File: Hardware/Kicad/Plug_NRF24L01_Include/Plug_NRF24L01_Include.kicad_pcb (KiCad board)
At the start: 2 copper layers, 55 x 40 mm, 43 parts, among them J1 Conn_01x07_Socket, Q1 2N7002, Q2 2N7002, Q3 2N7002, SW1 SW_Push, U1 NRF24L01, U2 AMS1117-3.3, U3 STM32L412KBTx, Y1 16 MHz

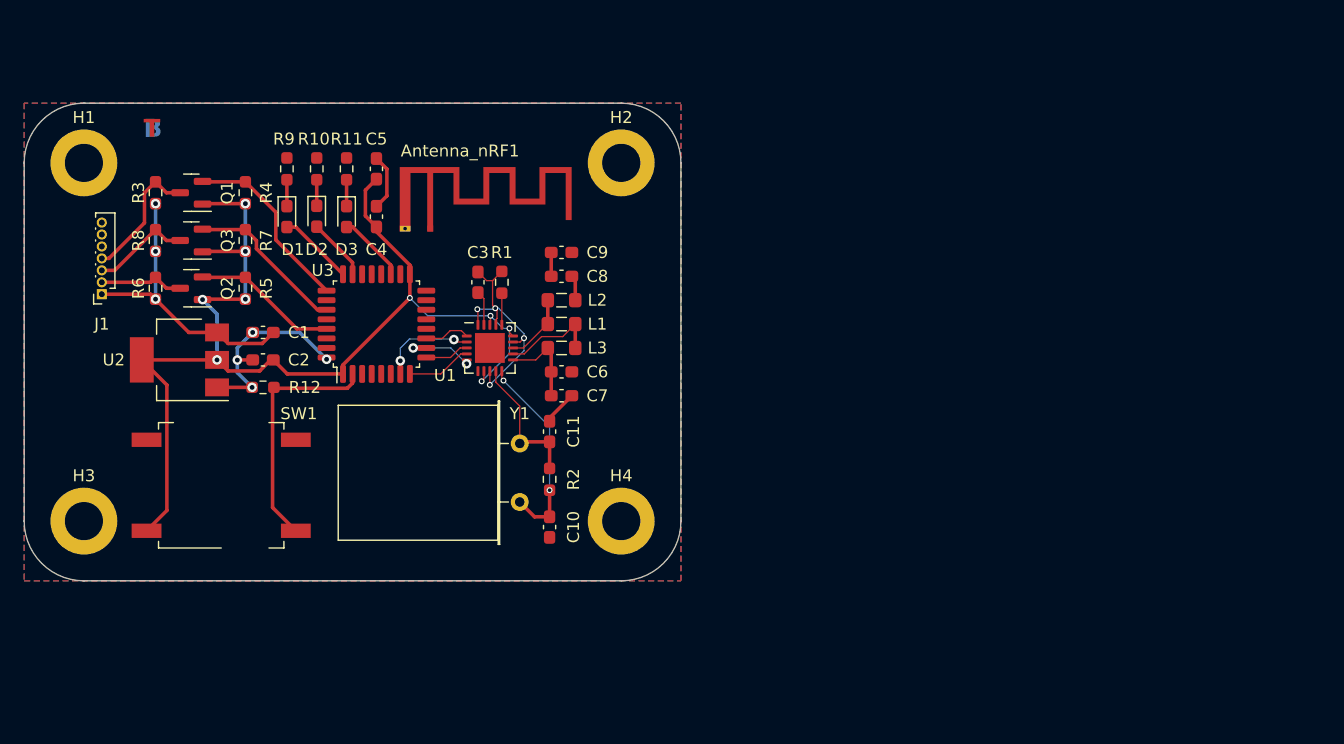
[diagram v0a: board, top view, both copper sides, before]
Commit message: Updated NRF24L01_Include
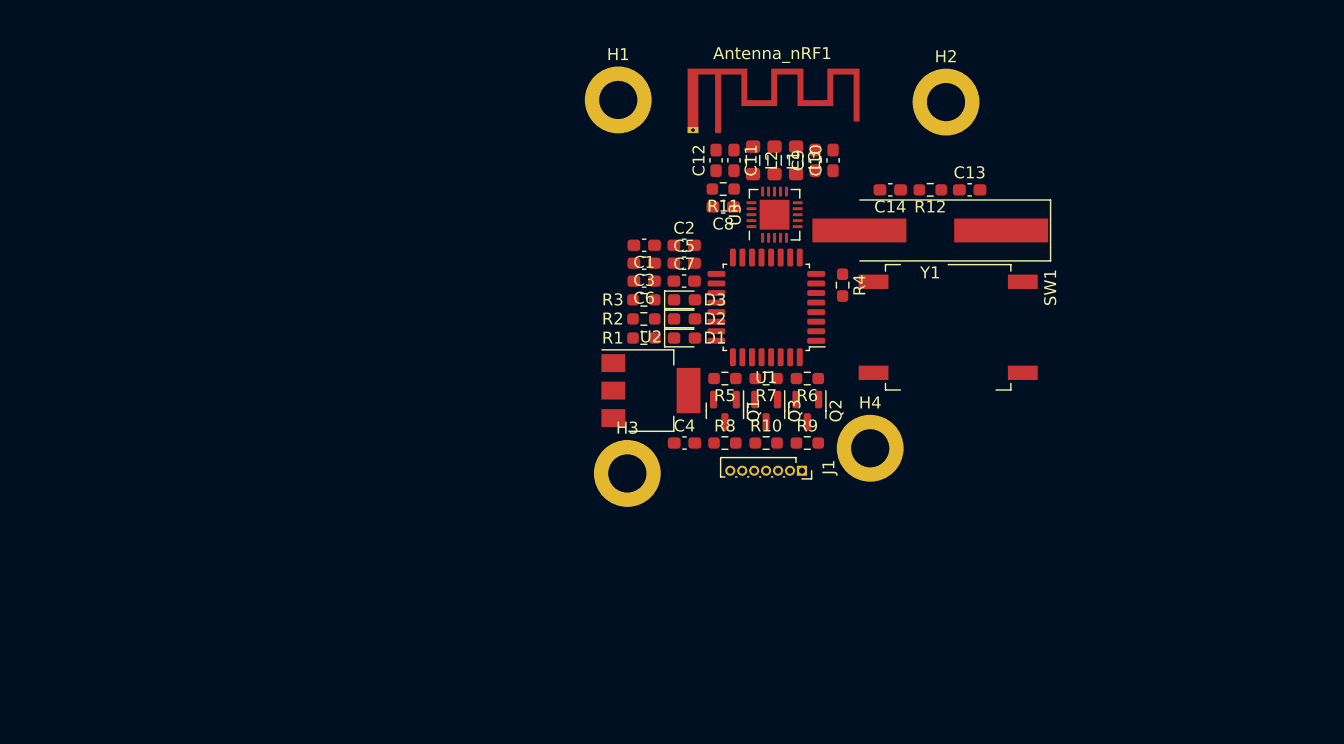
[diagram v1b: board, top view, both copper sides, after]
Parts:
- added C12: 1.0p, Capacitor_SMD:C_0603_1608Metric_Pad1.08x0.95mm_HandSolder, F.Cu at (100.9, 62.8)
- added C13: 22p, Capacitor_SMD:C_0603_1608Metric_Pad1.08x0.95mm_HandSolder, F.Cu at (122.2, 65.3)
- added C14: 22p, Capacitor_SMD:C_0603_1608Metric_Pad1.08x0.95mm_HandSolder, F.Cu at (115.5, 65.3)
- C1, C2: value 1u -> 100n
- C10: value 22p -> 4.7p
- C11: value 22p -> 1.5p
- C3: value 33n -> 100n
- C4: value 10n -> 1u
- C5: value 1n -> 1u
- C6: value 2.2n -> 10n
- C7: value 4.7p -> 1n
- C8: value 1.5p -> 33n
- C9: value 1.0p -> 2.2n
- R1: value 22k -> 1k
- R10, R9: value 1k -> 10k
- R11: value 1k -> 22k
- R12: value 10k -> 1M
- R2: value 1M -> 1k
- R3: value 10k -> 1k
- U1: value NRF24L01 -> STM32L412KBTx; footprint Package_DFN_QFN:QFN-20-1EP_4x4mm_P0.5mm_EP2.5x2.5mm -> Package_QFP:LQFP-32_7x7mm_P0.8mm
- U3: value STM32L412KBTx -> nRF24L01P; footprint Package_QFP:LQFP-32_7x7mm_P0.8mm -> Package_DFN_QFN:QFN-20-1EP_4x4mm_P0.5mm_EP2.5x2.5mm
- Y1: value 16 MHz -> 16MHz; footprint Crystal:Crystal_HC49-U_Horizontal -> Crystal:Crystal_SMD_HC49-SD_HandSoldering
- moved SW1 62.3 mm to (120.4, 76.8), turned to -90 degrees
- moved J1 60.5 mm to (108.1, 88.8), turned to -90 degrees
- moved R12 58.3 mm to (118.9, 65.3)
- moved R6 55.1 mm to (108.6, 81.1), turned to 180 degrees
- moved Q2 52.6 mm to (108.6, 83.8), turned to -90 degrees
- moved R4 50.6 mm to (111.5, 73.2), turned to -90 degrees
- moved R8 50.6 mm to (101.7, 86.5), turned to 0 degrees
- moved Q3 50.2 mm to (105.1, 83.8), turned to -90 degrees
- moved R9 49.3 mm to (108.6, 86.5), turned to 0 degrees
- moved Q1 48.3 mm to (101.7, 83.8), turned to -90 degrees
- moved H3 45.7 mm to (93.5, 89.0)
- moved R7 45.1 mm to (105.1, 81.1), turned to 180 degrees
- moved H1 45.1 mm to (92.8, 57.7)
- moved R10 44.1 mm to (105.1, 86.5), turned to 0 degrees
- moved R3 41.9 mm to (94.9, 74.5), turned to 180 degrees
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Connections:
- C1 pad 1: +5V -> +3.3V
- C10 pad 1: XC1 -> VDD_PA
- C11 pad 1: XC2 -> RF_Output
- C11 pad 2: GND -> Net-(C11-Pad2)
- C2 pad 1: VDD_NRF -> +3.3V
- C3 pad 1: Net-(U1-DVDD) -> +3.3V
- C3 pad 2: GND1 -> GND
- C4 pad 1: VDD_NRF -> +5V
- C5 pad 1: VDD_NRF -> +3.3V
- C6 pad 1: VDD_PA -> +3.3V
- C7 pad 1: VDD_PA -> +3.3V
- C8 pad 1: RF_Output -> Net-(U3-DVDD)
- C8 pad 2: Net-(C8-Pad2) -> GND1
- C9 pad 1: GND -> VDD_PA
- C9 pad 2: RF_Output -> GND
- L2 pad 2: Net-(C8-Pad2) -> Net-(C11-Pad2)
- Q1 pad 1: VDD_NRF -> +3.3V
- Q2 pad 1: VDD_NRF -> +3.3V
- Q3 pad 1: VDD_NRF -> +3.3V
- R1 pad 1: Net-(U1-IREF) -> Net-(D1-K)
- R1 pad 2: GND1 -> GND
- R10 pad 1: Net-(D2-K) -> +5V
- R10 pad 2: GND -> Data_Latch_SNES
- R11 pad 1: Net-(D3-K) -> Net-(U3-IREF)
- R11 pad 2: GND -> GND1
- R12 pad 1: Appairing_Btn -> XC1
- R12 pad 2: GND -> XC2
- R2 pad 1: XC1 -> Net-(D2-K)
- R2 pad 2: XC2 -> GND
- R3 pad 1: +5V -> Net-(D3-K)
- R3 pad 2: Serial_Data_SNES -> GND
- R4 pad 1: VDD_NRF -> Appairing_Btn
- R4 pad 2: Serial_Data_STM32 -> GND
- R5 pad 1: VDD_NRF -> +3.3V
- R5 pad 2: Data_Clock_STM32 -> Serial_Data_STM32
- R6 pad 1: +5V -> +3.3V
- R6 pad 2: Data_Clock_SNES -> Data_Clock_STM32
- R7 pad 1: VDD_NRF -> +3.3V
- R8 pad 2: Data_Latch_SNES -> Serial_Data_SNES
- R9 pad 1: Net-(D1-K) -> +5V
- R9 pad 2: GND -> Data_Clock_SNES
- SW1 pad 1: VDD_NRF -> +3.3V
- U1 pad 1: Chip_Enable -> +3.3V
- U1 pad 10: XC1 -> SPI_Digital_Output
- U1 pad 11: VDD_PA -> Chip_Enable
- U1 pad 12: ANT1 -> unconnected-(U1-PA6-Pad12)
- U1 pad 13: ANT2 -> unconnected-(U1-PA7-Pad13)
- U1 pad 14: GND1 -> unconnected-(U1-PB0-Pad14)
- U1 pad 15: VDD_NRF -> unconnected-(U1-PB1-Pad15)
- U1 pad 16: Net-(U1-IREF) -> GND
- U1 pad 17: GND1 -> +3.3V
- U1 pad 18: VDD_NRF -> unconnected-(U1-PA8-Pad18)
- U1 pad 19: Net-(U1-DVDD) -> Status_LED
- U1 pad 2: SPI_Chip_Select -> Appairing_Btn
- U1 pad 20: GND1 -> unconnected-(U1-PA10-Pad20)
- U1 pad 21: (no net) -> unconnected-(U1-PA11-Pad21)
- U1 pad 3: SPI_Clock -> unconnected-(U1-PC15-Pad3)
- U1 pad 4: SPI_Digital_Input -> unconnected-(U1-NRST-Pad4)
- U1 pad 5: SPI_Digital_Output -> +3.3V
- U1 pad 7: VDD_NRF -> SPI_Chip_Select
- U1 pad 8: GND1 -> SPI_Digital_Input
- U1 pad 9: XC2 -> SPI_Clock
- U2 pad 2: VDD_NRF -> +3.3V
- U3 pad 1: VDD_NRF -> Chip_Enable
- U3 pad 10: SPI_Digital_Output -> XC1
- U3 pad 11: Chip_Enable -> VDD_PA
- U3 pad 12: unconnected-(U3-PA6-Pad12) -> ANT1
- U3 pad 13: unconnected-(U3-PA7-Pad13) -> ANT2
- U3 pad 14: unconnected-(U3-PB0-Pad14) -> GND1
- U3 pad 15: unconnected-(U3-PB1-Pad15) -> +3.3V
- U3 pad 16: GND -> Net-(U3-IREF)
- U3 pad 17: VDD_NRF -> GND1
- U3 pad 18: unconnected-(U3-PA8-Pad18) -> +3.3V
- U3 pad 19: Status_LED -> Net-(U3-DVDD)
- U3 pad 2: Appairing_Btn -> SPI_Chip_Select
- U3 pad 20: unconnected-(U3-PA10-Pad20) -> GND1
- U3 pad 21: unconnected-(U3-PA11-Pad21) -> (no net)
- U3 pad 3: unconnected-(U3-PC15-Pad3) -> SPI_Clock
- U3 pad 4: unconnected-(U3-NRST-Pad4) -> SPI_Digital_Input
- U3 pad 5: +3.3VA -> SPI_Digital_Output
- U3 pad 7: SPI_Chip_Select -> +3.3V
- U3 pad 8: SPI_Digital_Input -> GND1
- U3 pad 9: SPI_Clock -> XC2
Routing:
- net VDD_NRF: track 96.2 -> 0.00 mm, vias 9 -> 0
- net GND: track 24.6 -> 0.00 mm, vias 4 -> 0
- net +5V: track 24.5 -> 0.00 mm, vias 3 -> 0
- net Appairing_Btn: track 20.4 -> 0.00 mm
- net GND1: track 20.3 -> 0.00 mm, vias 4 -> 0
- net XC1: track 16.9 -> 0.00 mm, vias 2 -> 0
- net Serial_Data_STM32: track 15.5 -> 0.00 mm
- net Data_Latch_STM32: track 13.6 -> 0.00 mm
- net Data_Clock_STM32: track 12.2 -> 0.00 mm
- net XC2: track 11.7 -> 0.00 mm
- net Serial_Data_SNES: track 11.1 -> 0.00 mm
- net Data_Latch_SNES: track 8.35 -> 0.00 mm
- net ANT1: track 8.25 -> 0.00 mm
- net SPI_Chip_Select: track 8.14 -> 0.00 mm, vias 2 -> 0
- net VDD_PA: track 7.45 -> 0.00 mm
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- removed copper zone on B.Cu, net GND
- removed copper zone on F.Cu, net GND
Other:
- board outline removed
- board text removed: "B"
- board text removed: "T"

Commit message: Updated Plug_NRF24L01_Include Schematic & Include (Added new components and modified footprints). Fixed some errors on NRF24L01_Exclude.
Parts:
- added C15: 100n, Capacitor_SMD:C_0603_1608Metric_Pad1.08x0.95mm_HandSolder, F.Cu at (135.6, 68.5)
- added D4: LED, Diode_SMD:D_0603_1608Metric_Pad1.05x0.95mm_HandSolder, F.Cu at (98.3, 73.0)
- added J2: Conn_02x07_Odd_Even, Connector_PinHeader_1.27mm:PinHeader_2x07_P1.27mm_Vertical_SMD, F.Cu at (142.6, 72.7)
- added Q4: 2N7002, Package_TO_SOT_SMD:SOT-23, F.Cu at (149.9, 69.4)
- added Q5: 2N7002, Package_TO_SOT_SMD:SOT-23, F.Cu at (149.9, 73.9)
- added R14: 10k, Resistor_SMD:R_0603_1608Metric_Pad0.98x0.95mm_HandSolder, F.Cu at (135.6, 71.0)
- added R15: 10k, Resistor_SMD:R_0603_1608Metric_Pad0.98x0.95mm_HandSolder, F.Cu at (135.6, 73.5)
- added R16: 10k, Resistor_SMD:R_0603_1608Metric_Pad0.98x0.95mm_HandSolder, F.Cu at (135.6, 76.0)
- added R17: 10k, Resistor_SMD:R_0603_1608Metric_Pad0.98x0.95mm_HandSolder, F.Cu at (135.6, 78.5)
- added R4: 1k, Resistor_SMD:R_0603_1608Metric_Pad0.98x0.95mm_HandSolder, F.Cu at (94.9, 73.0)
- C4: value 1u -> 470p
- C5: value 1u -> 2.2u
- U2: value AMS1117-3.3 -> MIC5219-3.3YMM; footprint Package_TO_SOT_SMD:SOT-223-3_TabPin2 -> Package_SO:MSOP-8_3x3mm_P0.65mm
- moved C4 6.90 mm to (98.4, 79.6), turned to 180 degrees
- moved C1 1.50 mm to (94.9, 68.4)
- moved C2 1.50 mm to (98.3, 68.4)
- moved C3 1.50 mm to (94.9, 69.9)
- moved C5 1.50 mm to (98.3, 69.9)
- moved C6 1.50 mm to (94.9, 71.4)
- moved C7 1.50 mm to (98.3, 71.4)
- moved U2 1.16 mm to (96.6, 82.4), turned to 180 degrees
- renumbered R9 to R10, R10 to R11, R11 to R12, R12 to R13, R4 to R5, R5 to R6, R6 to R7, R7 to R8, R8 to R9
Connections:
- C4 pad 1: +5V -> Net-(U2-BP)
- U1 pad 12: unconnected-(U1-PA6-Pad12) -> SPI_Digital_Input
- U1 pad 20: unconnected-(U1-PA10-Pad20) -> Player1_LED
- U1 pad 23: Player2_LED -> SWDIO
- U1 pad 24: Player1_LED -> SWDCK
- U1 pad 25: Serial_Data_STM32 -> Serial_Data1_STM32
- U1 pad 28: unconnected-(U1-PB5-Pad28) -> Serial_Data2_SNES
- U1 pad 30: unconnected-(U1-PB7-Pad30) -> IOBit_SNES
- U1 pad 4: unconnected-(U1-NRST-Pad4) -> NRST
- U1 pad 6: unconnected-(U1-PA0-Pad6) -> SPI_Clock
- U1 pad 8: SPI_Digital_Input -> USART2_TX
- U1 pad 9: SPI_Clock -> USART2_RX
- U2 pad 1: GND -> unconnected-(U2-EN-Pad1)
- U2 pad 2: +3.3V -> +5V
- U2 pad 3: +5V -> +3.3V

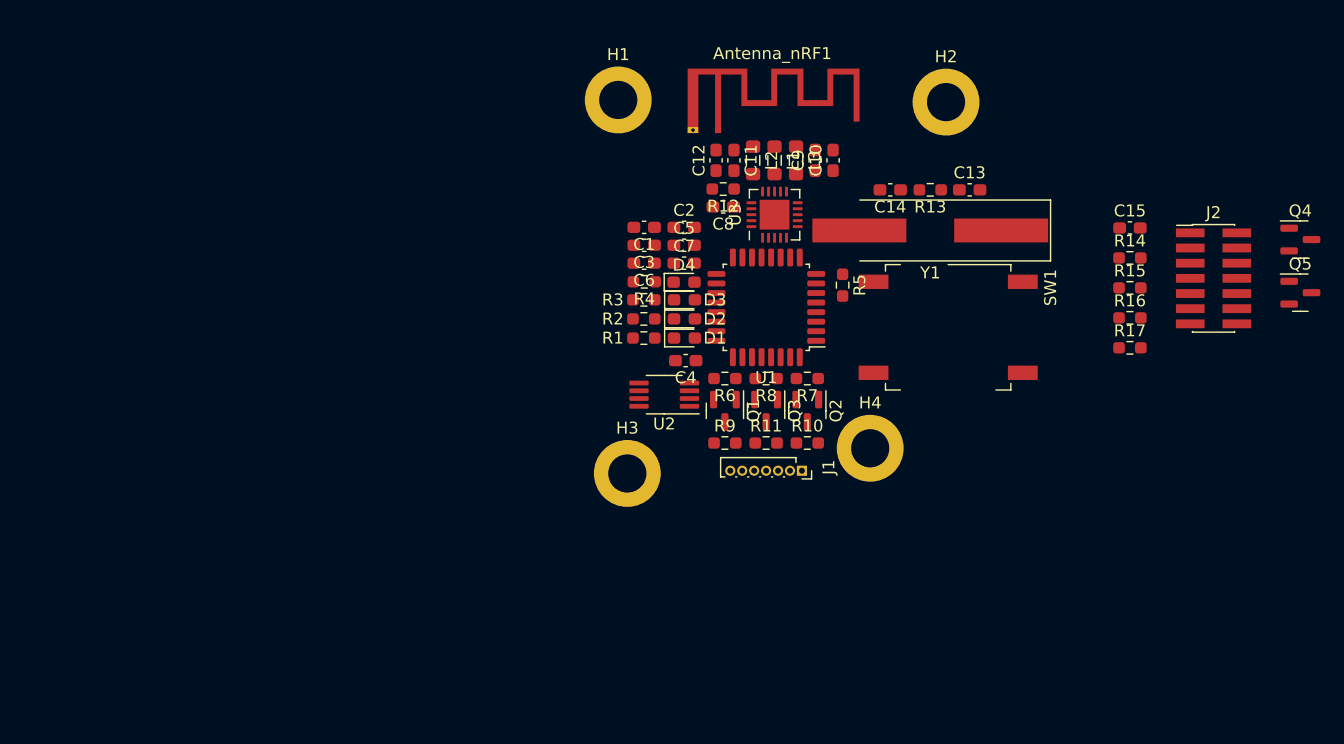
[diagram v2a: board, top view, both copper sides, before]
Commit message: Updated NRF24L01_Exclude PCB
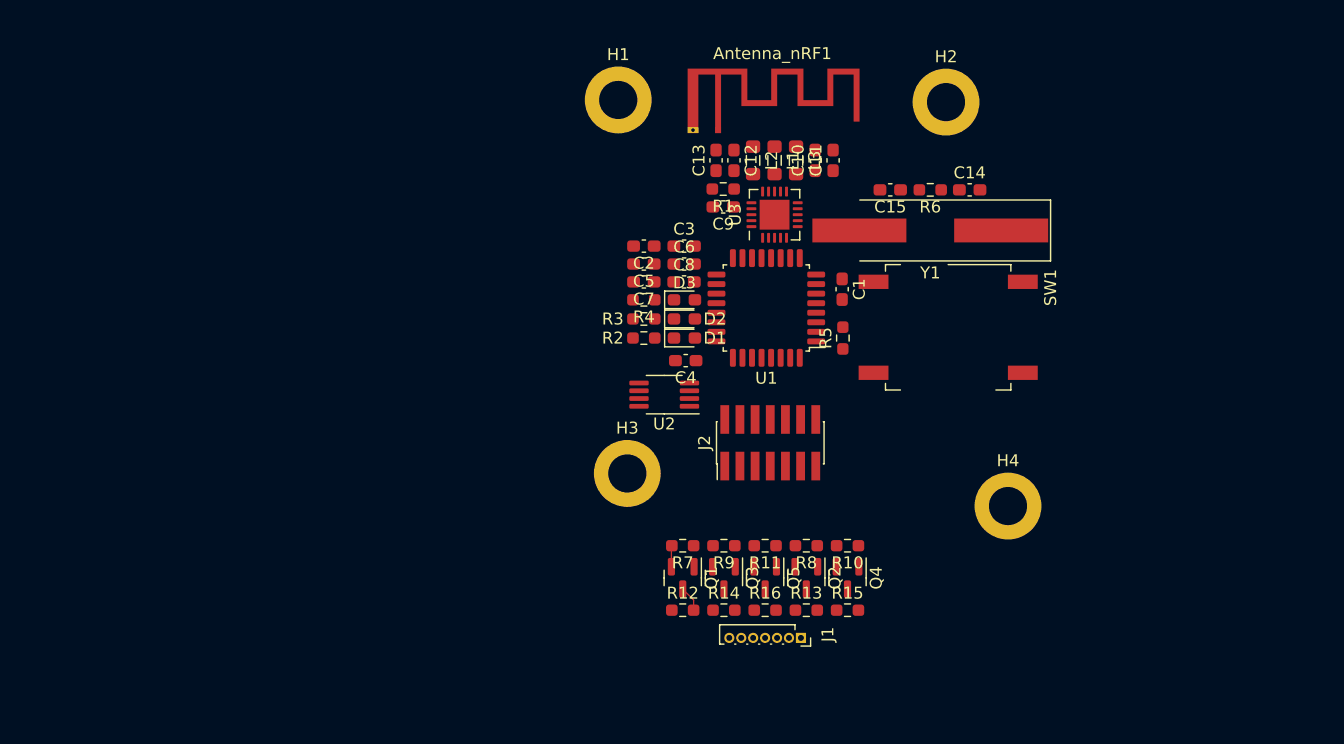
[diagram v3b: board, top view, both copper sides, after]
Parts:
- removed the D2 at (98.3, 76.1)
- removed the R2 at (94.9, 76.1)
- moved Q5 50.8 mm to (105.0, 97.8), turned to -90 degrees
- moved Q4 47.3 mm to (112.0, 97.8), turned to -90 degrees
- moved J2 39.6 mm to (105.5, 86.4), turned to 90 degrees
- moved R16 37.6 mm to (105.0, 100.5)
- moved R11 37.4 mm to (105.0, 95.1), turned to 180 degrees
- moved R15 34.0 mm to (112.0, 100.5)
- moved R10 33.8 mm to (112.0, 95.1), turned to 180 degrees
- moved C1 24.6 mm to (111.5, 73.6), turned to -90 degrees
- moved Q1 14.4 mm to (98.2, 97.8)
- moved Q3 14.4 mm to (101.6, 97.8)
- moved R12 14.4 mm to (98.2, 100.5)
- moved R14 14.4 mm to (101.6, 100.5)
- moved R7 14.4 mm to (98.2, 95.1)
- moved R9 14.4 mm to (101.6, 95.1)
- moved J1 14.0 mm to (108.0, 102.8)
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- renumbered C15 to C1, C9 to C10, C10 to C11, C11 to C12, C12 to C13, C13 to C14, C14 to C15, C1 to C2, C2 to C3, C3 to C5, C5 to C6, C6 to C7, C7 to C8, C8 to C9, D3 to D2, D4 to D3, R12 to R1, R14 to R10, R15 to R11, R9 to R12, R10 to R13, R11 to R14, R16 to R15, R17 to R16, R1 to R2, R13 to R6, R6 to R7, R7 to R8, R8 to R9
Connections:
- net Serial_Data_SNES renamed Serial_Data1_SNES
- J1 pad 5: unconnected-(J1-Pin_5-Pad5) -> Serial_Data2_SNES
- J1 pad 6: unconnected-(J1-Pin_6-Pad6) -> IOBit_SNES
- Q1 pad 2: Serial_Data_STM32 -> Serial_Data1_STM32
- R7 pad 2: Serial_Data_STM32 -> Serial_Data1_STM32
- U1 pad 28: Serial_Data2_SNES -> Serial_Data2_STM32
- U1 pad 30: IOBit_SNES -> IOBit_STM32
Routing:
- net Serial_Data1_SNES: track 0.00 -> 2.14 mm
- net Serial_Data1_STM32: track 0.00 -> 1.78 mm

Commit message: Updated PCB (Grouping and Tracks)
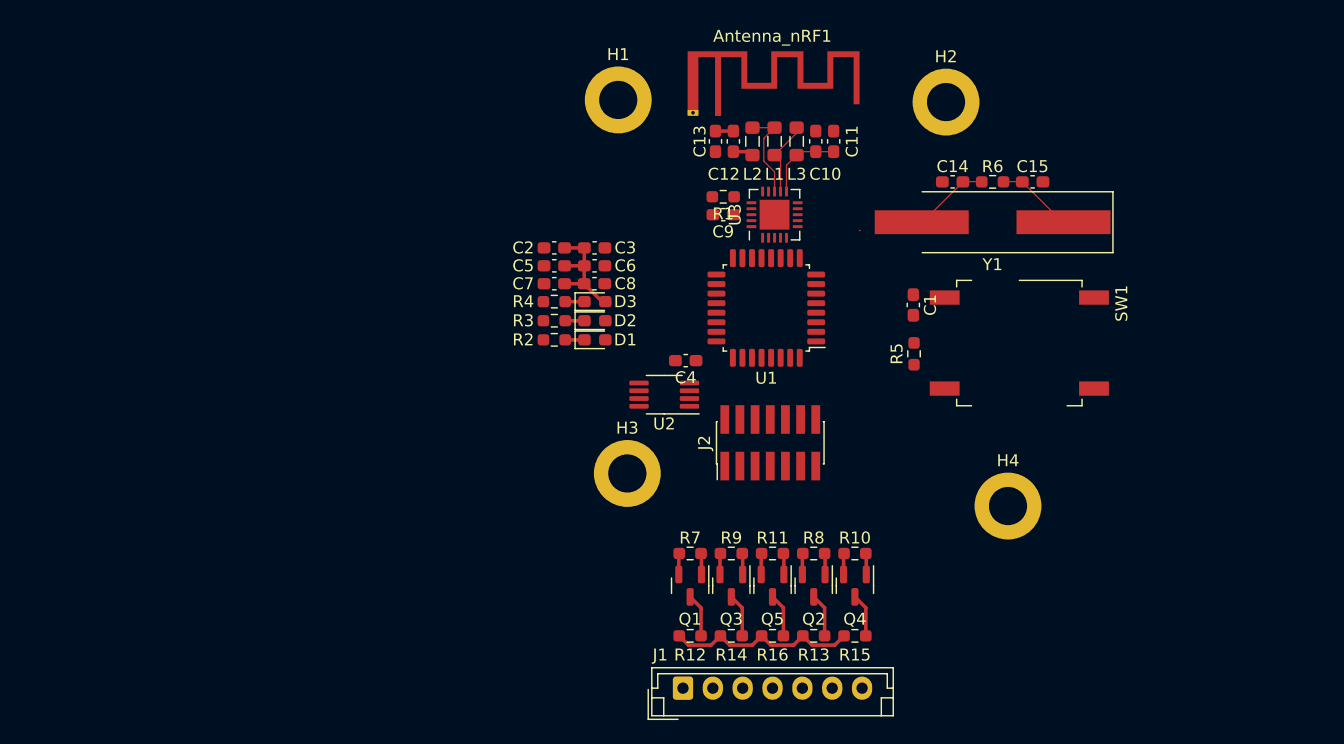
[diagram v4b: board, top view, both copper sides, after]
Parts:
- J1: footprint Connector_PinSocket_1.00mm:PinSocket_1x07_P1.00mm_Vertical -> Connector_JST:JST_EH_B7B-EH-A_1x07_P2.50mm_Vertical
- moved C15 11.9 mm to (127.5, 64.6), turned to 0 degrees
- moved J1 10.7 mm to (98.2, 107.0), turned to 0 degrees
- moved C2 7.50 mm to (87.4, 70.1)
- moved C3 7.50 mm to (90.8, 70.1)
- moved C5 7.50 mm to (87.4, 71.6)
- moved C6 7.50 mm to (90.8, 71.6)
- moved C7 7.50 mm to (87.4, 73.1)
- moved C8 7.50 mm to (90.8, 73.1)
- moved D1 7.50 mm to (90.8, 77.8)
- moved D2 7.50 mm to (90.8, 76.2)
- moved D3 7.50 mm to (90.8, 74.6)
- moved R2 7.50 mm to (87.4, 77.8)
- moved R3 7.50 mm to (87.4, 76.2)
- moved R4 7.50 mm to (87.4, 74.6)
- moved SW1 6.10 mm to (126.3, 78.1)
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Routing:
- net +3.3V: track 0.00 -> 19.2 mm
- net +5V: track 0.00 -> 16.4 mm
- net ANT2: track 0.00 -> 7.90 mm
- net VDD_PA: track 0.00 -> 6.62 mm
- net XC1: track 0.00 -> 6.43 mm
- net XC2: track 0.00 -> 6.43 mm
- net ANT1: track 0.00 -> 6.31 mm
- net IOBit_SNES: track 0.00 -> 3.64 mm
- net Serial_Data2_SNES: track 0.00 -> 3.64 mm
- net Data_Latch_SNES: track 0.00 -> 3.64 mm
- net Data_Clock_SNES: track 0.00 -> 3.64 mm
- net Data_Latch_STM32: track 0.00 -> 1.78 mm
- net Serial_Data2_STM32: track 0.00 -> 1.78 mm
- net IOBit_STM32: track 0.00 -> 1.78 mm
- net Data_Clock_STM32: track 0.00 -> 1.78 mm
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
